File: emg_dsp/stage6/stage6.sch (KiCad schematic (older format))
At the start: 170 parts, among them U1 RS232_CON, U10 EN_VDD, U11 USBLC6, U12 ABM10XTAL, U13 BF527, U14 AT25DF041-MHF, U15 ADSP_JTAG_CON, U16 LAN8710A, U17 74LCX541, U18 SFE-MAGJACK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

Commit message: ethernet partially routed, SDRAM mostly / completely routed. getting there!
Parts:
- R10, R11, R12, R9: value 50k -> 22k
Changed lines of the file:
@@
-EESchema Schematic File Version 2  date Tue 28 Sep 2010 03:06:55 PM EDT
+EESchema Schematic File Version 2  date Tue 28 Sep 2010 06:55:35 PM EDT
 LIBS:power
 LIBS:device
@@
 P 6500 3250
 F 0 "R12" V 6500 3350 50  0000 C CNN
-F 1 "50k" V 6500 3200 50  0000 C CNN
+F 1 "22k" V 6500 3200 50  0000 C CNN
 F 2 "0402" V 6500 3750 60  0001 C CNN
 	1    6500 3250
@@
 P 6500 3150
 F 0 "R11" V 6500 3250 50  0000 C CNN
-F 1 "50k" V 6500 3100 50  0000 C CNN
+F 1 "22k" V 6500 3100 50  0000 C CNN
 F 2 "0402" V 6500 3650 60  0001 C CNN
 	1    6500 3150
@@
 P 6500 3050
 F 0 "R10" V 6500 3150 50  0000 C CNN
-F 1 "50k" V 6500 3000 50  0000 C CNN
+F 1 "22k" V 6500 3000 50  0000 C CNN
 F 2 "0402" V 6500 3550 60  0001 C CNN
 	1    6500 3050
@@
 P 6500 2950
 F 0 "R9" V 6500 3050 50  0000 C CNN
-F 1 "50k" V 6500 2900 50  0000 C CNN
+F 1 "22k" V 6500 2900 50  0000 C CNN
 F 2 "0402" V 6500 3450 60  0001 C CNN
 	1    6500 2950

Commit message: wired, wireless, some of bridge are routed. next up is the EMG system.
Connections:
- net GND: now also C42.2, C44.2, U18.100 (SHIELD), U18.101 (SHIELD2), U18.102 (SHEILD3), U18.103 (SHEILD4)
- net VDD: now also C42.1, C44.1

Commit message: added audio out to both the wireless-emg and bridge -- very simple circut, sholud work.  layout maybe 70% done.
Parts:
- C1: footprint 2x100mil -> 2917
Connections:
- net audioout/TFS: now reaches U13.A3 (PF11-TFS1)
- net audioout/TCLK: now reaches U13.A5 (PF13-TSCLK1)
- net audioout/DTPRI: now reaches U13.B5 (PF12-DT1PRI)
- no-connect marks 32 -> 29

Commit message: submitted a (partial) BOM .. !! board is not yet cone, but at least we now know to switch the footprint on the flash.
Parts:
- U12: value ABM10XTAL -> ABM10XTAL-24
- U14: footprint UFDN-8 -> SOIC-8
- U9: value ABM10XTAL -> ABM10XTAL-25
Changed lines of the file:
@@
-EESchema Schematic File Version 2  date Thu 30 Sep 2010 05:10:58 PM EDT
+EESchema Schematic File Version 2  date Thu 30 Sep 2010 11:24:56 PM EDT
 LIBS:power
 LIBS:device
@@
 Sheet 1 15
 Title "Stage 4 / Copyright 2010 Timothy L Hanson "
-Date "30 sep 2010"
+Date "1 oct 2010"
 Rev ""
 Comp "This design is free: redistribute or modify under the GPL v. 3 or later"
@@
 P 5150 5450
 F 0 "U9" H 5150 5600 60  0000 C CNN
-F 1 "ABM10XTAL" H 5200 5300 60  0000 C CNN
+F 1 "ABM10XTAL-25" H 5200 5300 60  0000 C CNN
 F 2 "ABM10" H 4900 5600 60  0000 C CNN
 	1    5150 5450
@@
 F 0 "U14" H 10150 450 60  0000 C CNN
 F 1 "AT25DF041-MHF" H 10150 1000 60  0000 C CNN
-F 2 "UFDN-8" H 10210 390 60  0000 C CNN
+F 2 "SOIC-8" H 10210 390 60  0000 C CNN
 	1    10100 700
 	1    0    0    -1
@@
 P 5900 4400
 F 0 "U12" H 5900 4550 60  0000 C CNN
-F 1 "ABM10XTAL" H 5950 4250 60  0000 C CNN
+F 1 "ABM10XTAL-24" H 5950 4250 60  0000 C CNN
 F 2 "ABM10" H 5650 4550 60  0000 C CNN
 	1    5900 4400

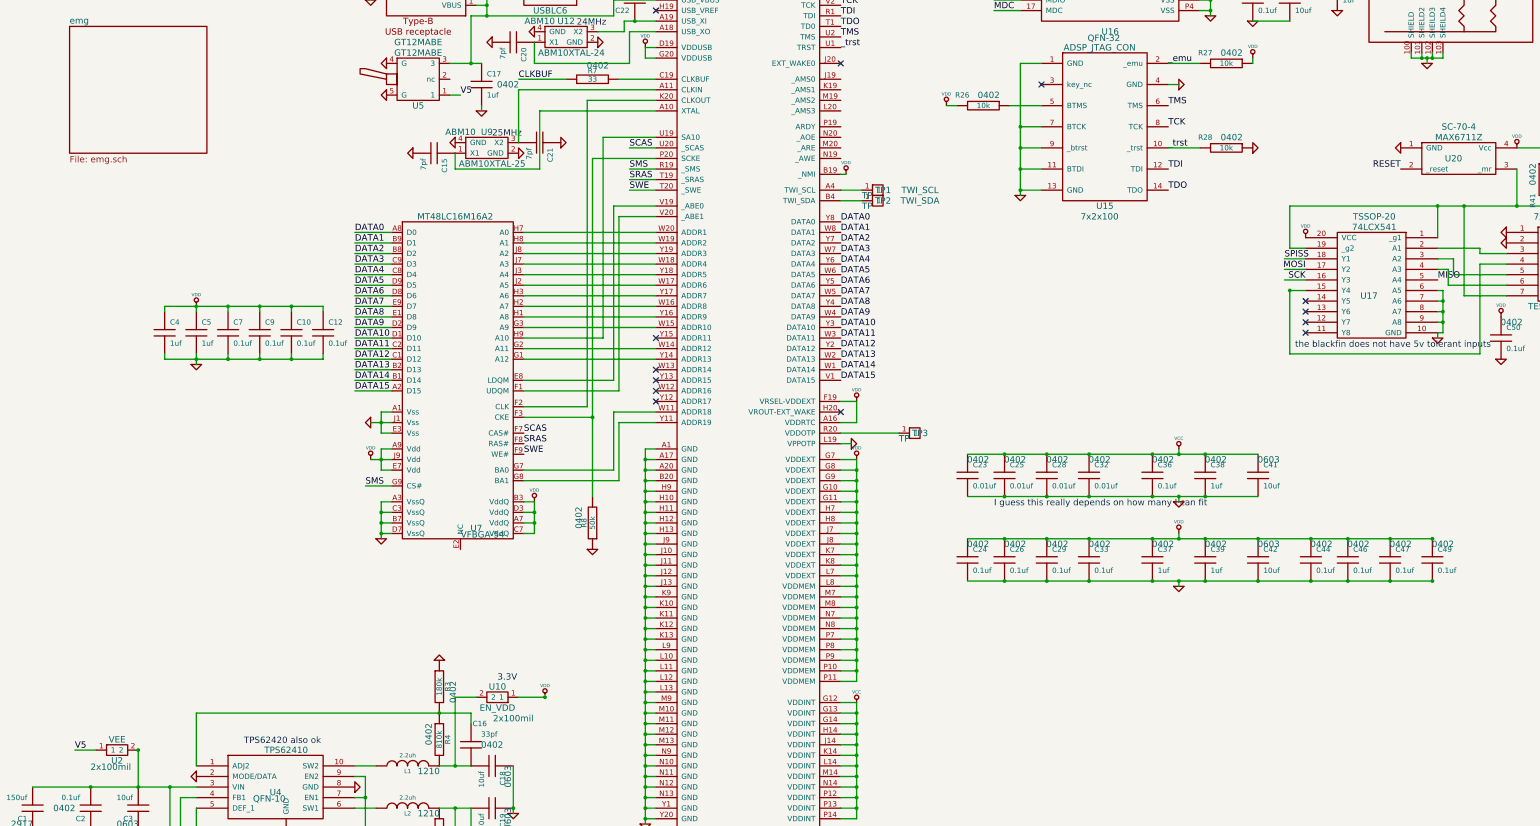
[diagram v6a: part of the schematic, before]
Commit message: getting the last of the nets (GND, Vdd, Vcc) routed. still need to check the pinouts, etc.
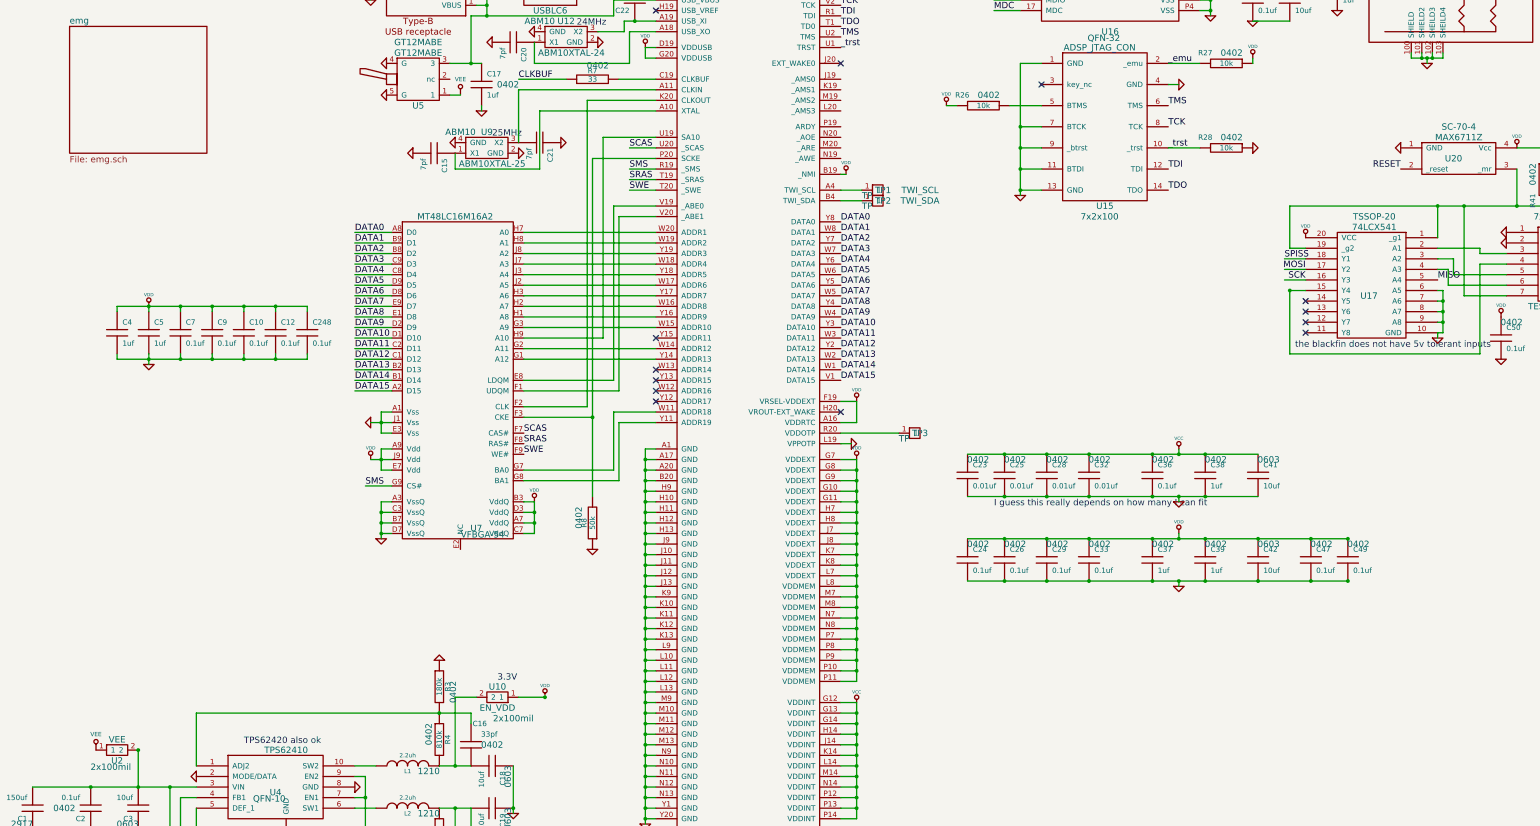
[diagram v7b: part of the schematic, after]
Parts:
- removed C44, C46: 0.1uf, 0402, symbol C
- added C248: 0.1uf, 0402, symbol C
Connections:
- net V5 is gone; now on net VEE: U2.1, U5.1
- net GND: now also C248.2
- net VDD: now also C248.1
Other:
- moved on the sheet: C10, C12, C4, C47, C49, C5, C7, C9

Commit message: board getting done! next up is silkscreen - pita.
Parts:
- added TP64, TP65, TP66, TP67: TP, 2.9mm_hole, symbol TP
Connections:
- net GND: now also TP64.1, TP65.1, TP66.1, TP67.1
